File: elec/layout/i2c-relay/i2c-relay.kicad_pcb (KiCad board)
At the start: 2 copper layers, 7 parts, among them U2 10kΩ ±1% 62.5mW, U3 1kΩ ±1% 62.5mW

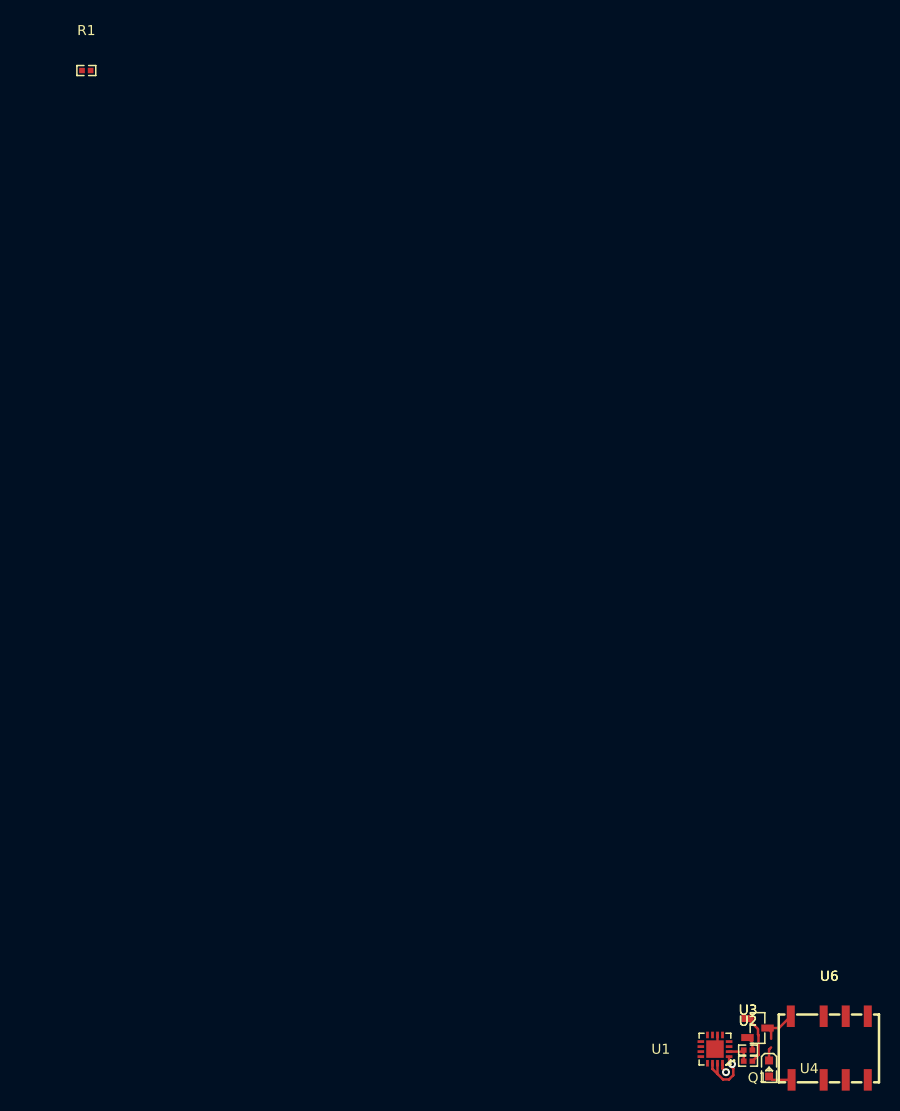
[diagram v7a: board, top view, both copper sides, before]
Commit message: fix build errors, add output connectors
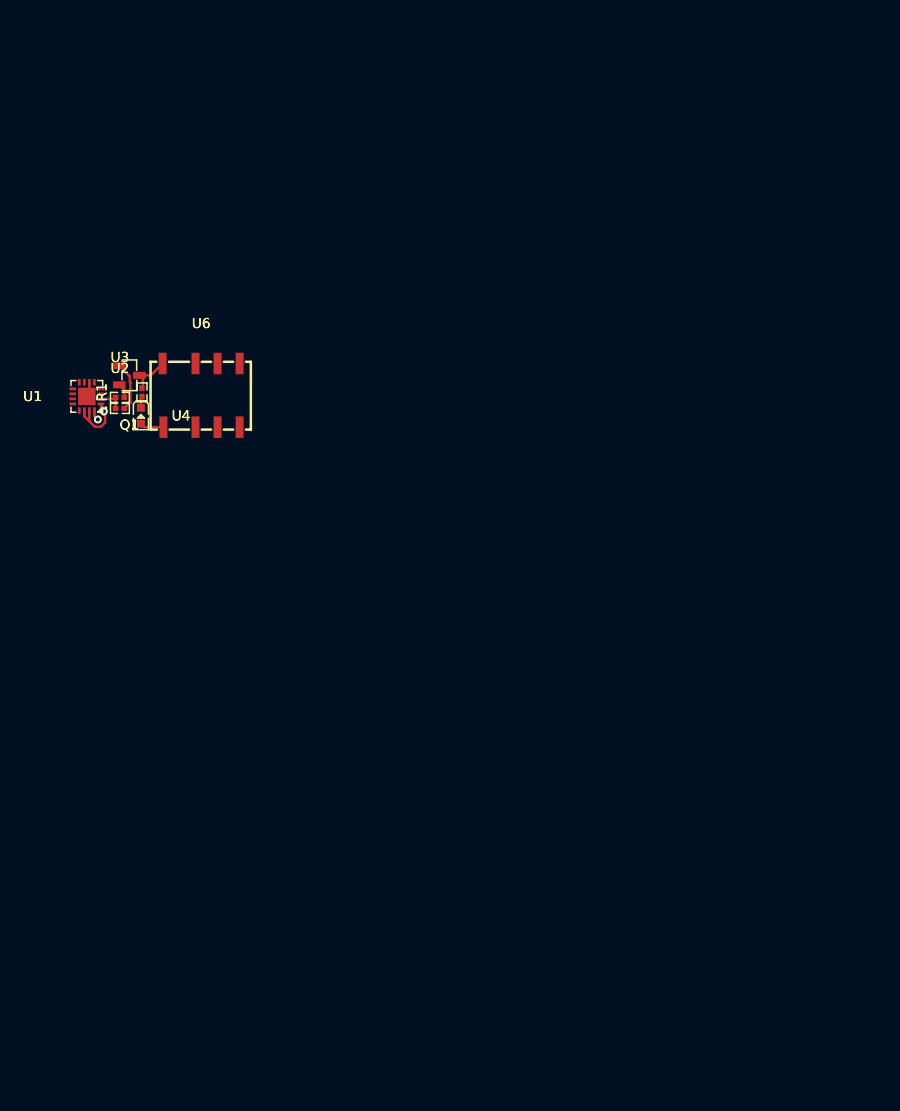
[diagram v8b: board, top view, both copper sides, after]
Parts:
- moved Q1 90.3 mm to (64.3, 25.4)
- moved U1 90.3 mm to (60.0, 27.5)
- moved U2 90.3 mm to (63.4, 28.7)
- moved U3 90.3 mm to (63.4, 27.6)
- moved U4 90.3 mm to (65.4, 29.4)
- moved U6 90.3 mm to (71.5, 27.4)
- moved R1 32.6 mm to (65.5, 27.1), turned to 90 degrees
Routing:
- net (no net): track 5.42 -> 0.00 mm
- net relay-gnd: track 0.00 -> 4.03 mm
- net cathode: track 0.00 -> 1.39 mm
